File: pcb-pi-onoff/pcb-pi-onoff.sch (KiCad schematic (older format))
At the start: 27 parts, among them J1 Conn_02x20_Odd_Even, J3 Conn_01x06_Male, J4 USB_B_Micro, J5 RUN/~PGM~, J6 Conn_01x03_Male, J7 Conn_SW1, J8 Conn_01x02_Bat, Q1 AO3401A, SW1 SW_Push, U1 TSOP4838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

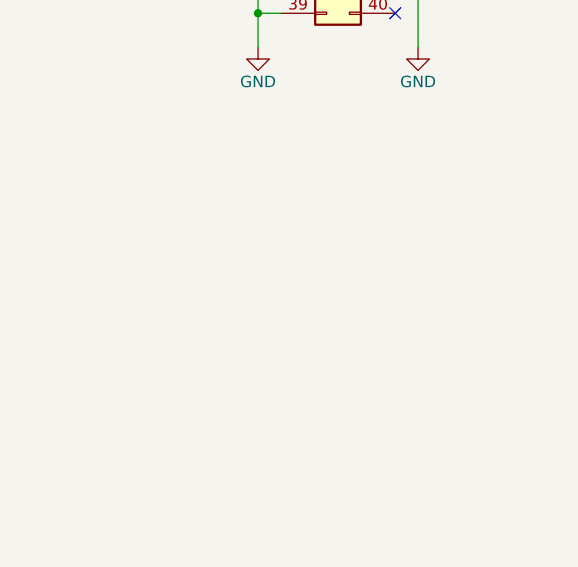
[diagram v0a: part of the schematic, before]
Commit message: added I2C-connector
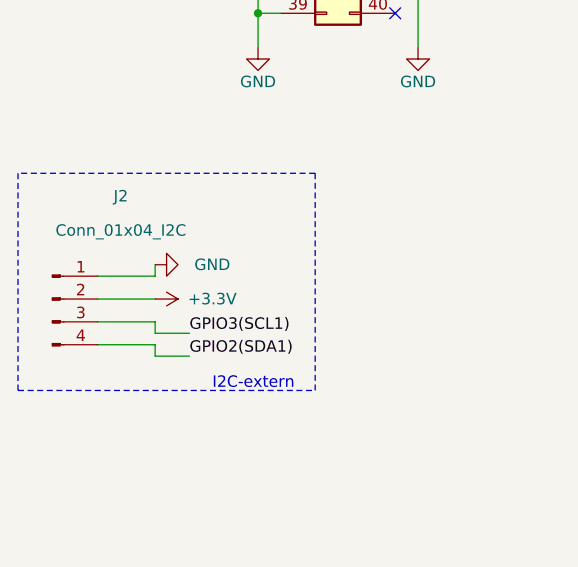
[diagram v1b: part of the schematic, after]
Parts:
- added J2: Conn_01x04_I2C, Connector_PinHeader_2.54mm:PinHeader_1x04_P2.54mm_Vertical, symbol Connector:Conn_01x04_Male
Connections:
- net +3V3: now also J2.2 (Pin_2)
- net GND: now also J2.1 (Pin_1)
- net GPIO2(SDA1): now also J2.4 (Pin_4)
- net GPIO3(SCL1): now also J2.3 (Pin_3)
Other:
- note added: "I2C-extern"
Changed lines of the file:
@@
 $EndComp
 Connection ~ 6100 3100
+$Comp
+L Connector:Conn_01x04_Male J2
+U 1 1 60BFEDEF
+P 800 4100
+F 0 "J2" H 1100 4550 50  0000 C CNN
+F 1 "Conn_01x04_I2C" H 1100 4400 50  0000 C CNN
+F 2 "Connector_PinHeader_2.54mm:PinHeader_1x04_P2.54mm_Vertical" H 800 4100 50  0001 C CNN
+F 3 "~" H 800 4100 50  0001 C CNN
+	1    800  4100
+	1    0    0    -1
+$EndComp
+$Comp
+L power:GND #PWR0106
+U 1 1 60BFFA58
+P 1250 3950
+F 0 "#PWR0106" H 1250 3700 50  0001 C CNN
+F 1 "GND" V 1250 3700 50  0000 C CNN
+F 2 "" H 1250 3950 50  0001 C CNN
+F 3 "" H 1250 3950 50  0001 C CNN
+	1    1250 3950
+	0    -1   -1   0
+$EndComp
+$Comp
+L power:+3.3V #PWR0107
+U 1 1 60C00252
+P 1250 4100
+F 0 "#PWR0107" H 1250 3950 50  0001 C CNN
+F 1 "+3.3V" V 1250 4350 50  0000 C CNN
+F 2 "" H 1250 4100 50  0000 C CNN
+F 3 "" H 1250 4100 50  0000 C CNN
+	1    1250 4100
+	0    1    1    0
+$EndComp
+Text Label 1400 4250 0    50   ~ 0
+GPIO3(SCL1)
+Text Label 1400 4350 0    50   ~ 0
+GPIO2(SDA1)
+Wire Wire Line
+	1000 4000 1250 4000
+Wire Wire Line
+	1000 4100 1250 4100
+Wire Wire Line
+	1000 4200 1250 4200
+Wire Wire Line
+	1250 4200 1250 4250
+Wire Wire Line
+	1000 4300 1250 4300
+Wire Wire Line
+	1250 4300 1250 4350
+Wire Wire Line
+	1250 4000 1250 3950
+Wire Wire Line
+	1250 4250 1400 4250
+Wire Wire Line
+	1250 4350 1400 4350
+Wire Notes Line
+	650  3550 650  4500
+Wire Notes Line
+	650  4500 1950 4500
+Wire Notes Line
+	1950 4500 1950 3550
+Wire Notes Line
+	1950 3550 650  3550
+Text Notes 1500 4500 0    50   ~ 0
+I2C-extern
 $EndSCHEMATC

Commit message: added SPI-connector
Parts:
- added J9: Conn_01x06_SPI, Connector_PinHeader_2.54mm:PinHeader_1x06_P2.54mm_Vertical, symbol Connector:Conn_01x06_Male
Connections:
- net +3V3: now also J9.6 (Pin_6)
- net GND: now also J9.5 (Pin_5)
- net GPIO10(SPI-TX): now reaches J1.19 (Pin_19)
- net GPIO10(SPI-TX): now also J9.3 (Pin_3)
- net GPIO9(SPI-RX): now reaches J1.21 (Pin_21)
- net GPIO9(SPI-RX): now also J9.1 (Pin_1)
- net GPIO11(SPI-CLK): now reaches J1.23 (Pin_23)
- net GPIO11(SPI-CLK): now also J9.4 (Pin_4)
- net GPIO8(SPI-CE0): now reaches J1.24 (Pin_24)
- net GPIO8(SPI-CE0): now also J9.2 (Pin_2)
- no-connect marks 30 -> 26
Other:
- note added: "SPI-extern"
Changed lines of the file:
@@
 NoConn ~ 2300 1750
 NoConn ~ 2300 1950
-NoConn ~ 2300 2050
 NoConn ~ 2300 2150
 NoConn ~ 2300 2250
@@
 NoConn ~ 1800 2350
 NoConn ~ 1800 2250
-NoConn ~ 1800 2050
-NoConn ~ 1800 1950
-NoConn ~ 1800 1850
 NoConn ~ 1800 1650
 NoConn ~ 1800 1550
@@
 Text Notes 1500 4500 0    50   ~ 0
 I2C-extern
+Wire Wire Line
+	650  1850 1800 1850
+Text Label 650  1850 0    50   ~ 0
+GPIO10(SPI-TX)
+Wire Wire Line
+	650  1950 1800 1950
+Text Label 650  1950 0    50   ~ 0
+GPIO9(SPI-RX)
+Wire Wire Line
+	650  2050 1800 2050
+Text Label 650  2050 0    50   ~ 0
+GPIO11(SPI-CLK)
+Wire Wire Line
+	3450 2050 2300 2050
+Text Label 3450 2050 2    50   ~ 0
+GPIO8(SPI-CE0)
+$Comp
+L Connector:Conn_01x06_Male J9
+U 1 1 60C64E02
+P 2500 4100
+F 0 "J9" H 2750 4550 50  0000 C CNN
+F 1 "Conn_01x06_SPI" H 2800 4450 50  0000 C CNN
+F 2 "Connector_PinHeader_2.54mm:PinHeader_1x06_P2.54mm_Vertical" H 2500 4100 50  0001 C CNN
+F 3 "~" H 2500 4100 50  0001 C CNN
+	1    2500 4100
+	1    0    0    -1
+$EndComp
+Text Label 3050 3900 0    50   ~ 0
+GPIO9(SPI-RX)
+Text Label 3050 4000 0    50   ~ 0
+GPIO8(SPI-CE0)
+Text Label 3050 4100 0    50   ~ 0
+GPIO10(SPI-TX)
+Text Label 3050 4200 0    50   ~ 0
+GPIO11(SPI-CLK)
+$Comp
+L power:GND #PWR02
+U 1 1 60C65E52
+P 3050 4300
+F 0 "#PWR02" H 3050 4050 50  0001 C CNN
+F 1 "GND" V 3050 4050 50  0000 C CNN
+F 2 "" H 3050 4300 50  0001 C CNN
+F 3 "" H 3050 4300 50  0001 C CNN
+	1    3050 4300
+	0    -1   -1   0
+$EndComp
+$Comp
+L power:+3.3V #PWR018
+U 1 1 60C6639C
+P 3050 4400
+F 0 "#PWR018" H 3050 4250 50  0001 C CNN
+F 1 "+3.3V" V 3050 4650 50  0000 C CNN
+F 2 "" H 3050 4400 50  0000 C CNN
+F 3 "" H 3050 4400 50  0000 C CNN
+	1    3050 4400
+	0    1    1    0
+$EndComp
+Wire Wire Line
+	2700 3900 3050 3900
+Wire Wire Line
+	2700 4000 3050 4000
+Wire Wire Line
+	2700 4100 3050 4100
+Wire Wire Line
+	2700 4200 3050 4200
+Wire Wire Line
+	2700 4300 3050 4300
+Wire Wire Line
+	2700 4400 3050 4400
+Wire Notes Line
+	2400 3550 2400 4500
+Wire Notes Line
+	2400 4500 3900 4500
+Wire Notes Line
+	3900 4500 3900 3550
+Wire Notes Line
+	3900 3550 2400 3550
+Text Notes 3450 4500 0    50   ~ 0
+SPI-extern
 $EndSCHEMATC

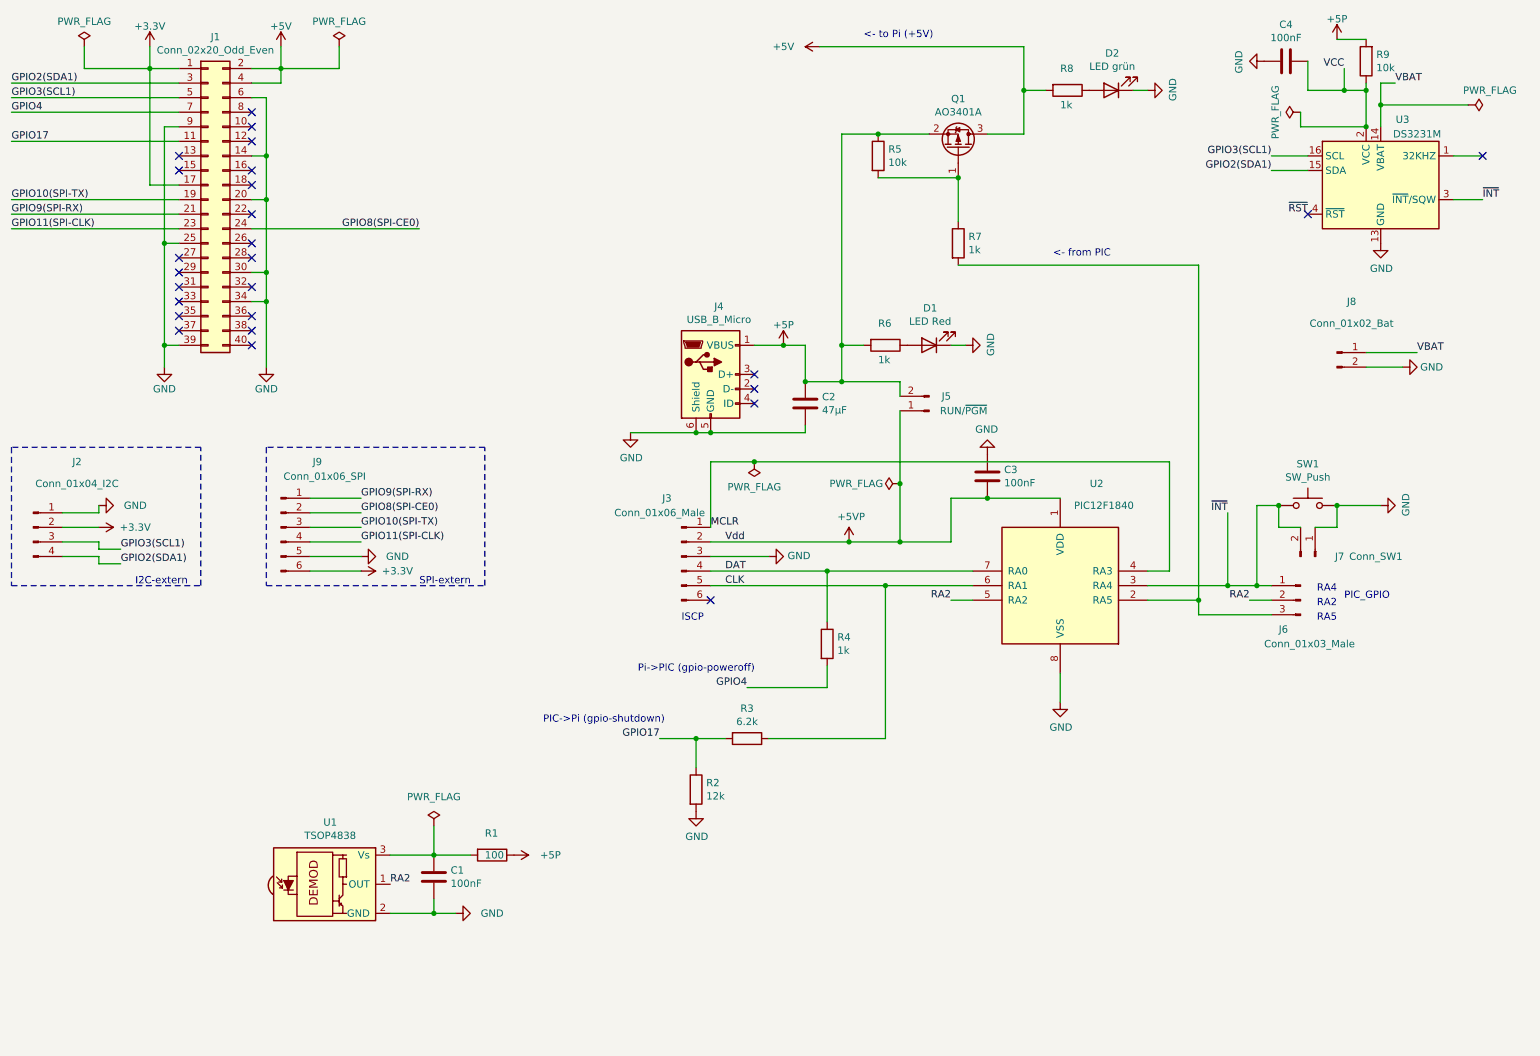
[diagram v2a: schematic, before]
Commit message: added GPIO-connector
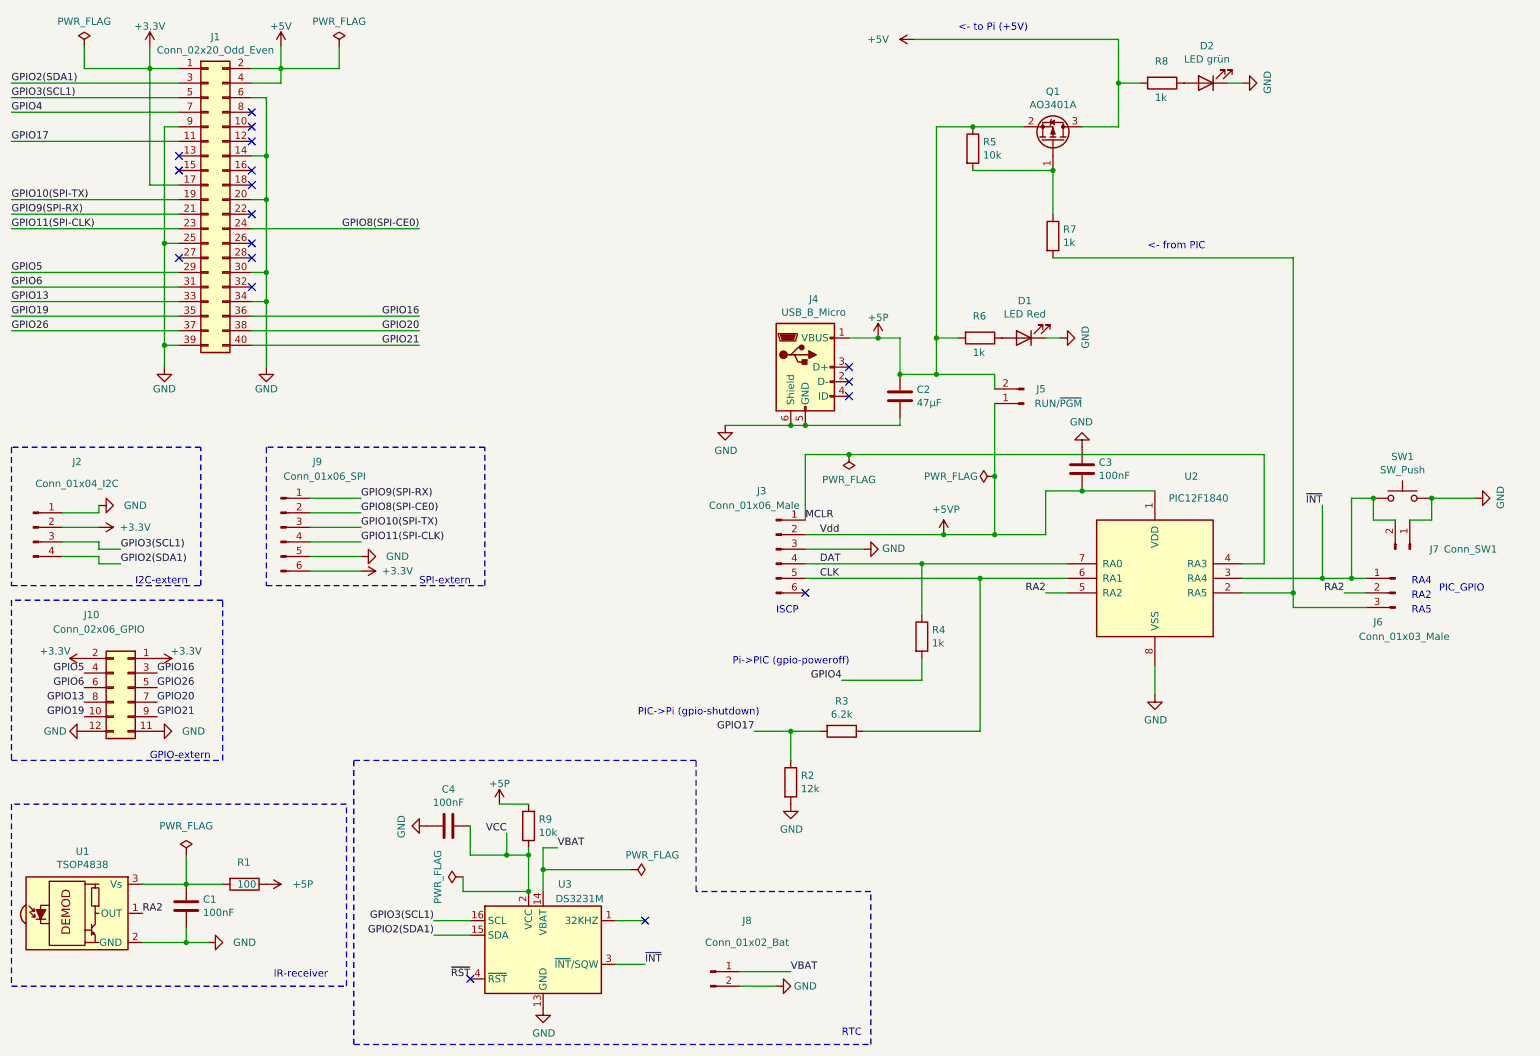
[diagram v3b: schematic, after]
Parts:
- added J10: Conn_02x06_GPIO, Connector_PinHeader_2.54mm:PinHeader_2x06_P2.54mm_Vertical, symbol Connector_Generic:Conn_02x06_Odd_Even
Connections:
- net +3V3: now also J10.1 (Pin_1), J10.2 (Pin_2)
- net GND: now also J10.11 (Pin_11), J10.12 (Pin_12)
- net GPIO5: now reaches J1.29 (Pin_29)
- net GPIO5: now also J10.4 (Pin_4)
- net GPIO6: now reaches J1.31 (Pin_31)
- net GPIO6: now also J10.6 (Pin_6)
- net GPIO13: now reaches J1.33 (Pin_33)
- net GPIO13: now also J10.8 (Pin_8)
- net GPIO19: now reaches J1.35 (Pin_35)
- net GPIO19: now also J10.10 (Pin_10)
- net GPIO16: now reaches J1.36 (Pin_36)
- net GPIO16: now also J10.3 (Pin_3)
- net GPIO26: now reaches J1.37 (Pin_37)
- net GPIO26: now also J10.5 (Pin_5)
- net GPIO20: now reaches J1.38 (Pin_38)
- net GPIO20: now also J10.7 (Pin_7)
- net GPIO21: now reaches J1.40 (Pin_40)
- net GPIO21: now also J10.9 (Pin_9)
- no-connect marks 26 -> 18
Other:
- note added: "GPIO-extern"
- note added: "IR-receiver"
- note added: "RTC"
- moved on the sheet: C1, C2, C3, C4, D1, D2, J3, J4, J5, J6, J7, J8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

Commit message: replaced footprints for PIC and RTC with handsolder-version
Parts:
- U2: footprint Package_SO:SO-8_3.9x4.9mm_P1.27mm -> user:SO-8_3.9x4.9mm_P1.27mm_HandSolder
- U3: footprint Package_SO:SOIC-16W_7.5x10.3mm_P1.27mm -> user:SOIC-16W_7.5x10.3mm_P1.27mm_HandSolder
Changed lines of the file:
@@
 F 0 "U2" H 8750 5150 50  0000 C CNN
 F 1 "PIC12F1840" H 8800 5000 50  0000 C CNN
-F 2 "Package_SO:SO-8_3.9x4.9mm_P1.27mm" H 9100 5100 50  0001 C CNN
+F 2 "user:SO-8_3.9x4.9mm_P1.27mm_HandSolder" H 9100 5100 50  0001 C CNN
 F 3 "" H 8500 4450 50  0001 C CNN
 	1    8500 4450
@@
 F 0 "U3" H 4450 7450 50  0000 C CNN
 F 1 "DS3231M" H 4550 7350 50  0000 C CNN
-F 2 "Package_SO:SOIC-16W_7.5x10.3mm_P1.27mm" H 4300 6400 50  0001 C CNN
+F 2 "user:SOIC-16W_7.5x10.3mm_P1.27mm_HandSolder" H 4300 6400 50  0001 C CNN
 F 3 "http://datasheets.maximintegrated.com/en/ds/DS3231.pdf" H 4570 7050 50  0001 C CNN
 	1    4300 7000

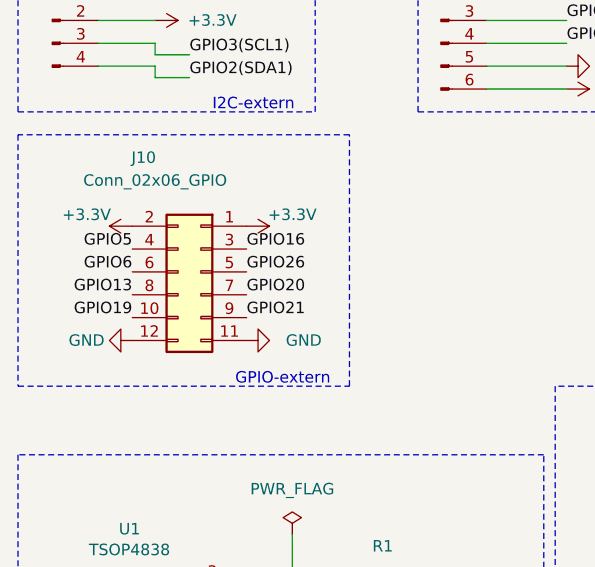
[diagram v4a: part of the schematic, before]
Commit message: Rev 1.0: changed 3V3/GND on GPIO-connector
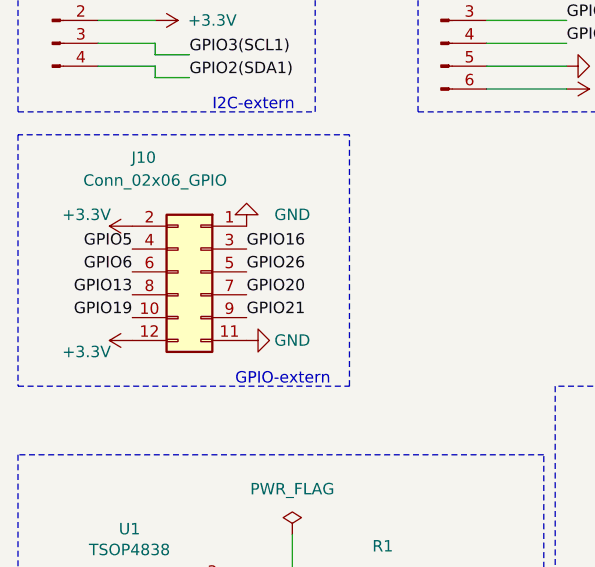
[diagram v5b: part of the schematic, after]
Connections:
- net +3V3: now also J10.12 (Pin_12); no longer J10.1 (Pin_1)
- net GND: now also J10.1 (Pin_1); no longer J10.12 (Pin_12)
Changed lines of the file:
@@
 Sheet 1 1
 Title "Pi OnOff Hat"
-Date "2021-06-08"
-Rev "0.9"
+Date "2021-06-09"
+Rev "1.0"
 Comp "Bernhard Bablok"
 Comment1 "https://github.com/bablokb/pcb-pi-onoff"
@@
 L power:GND #PWR0108
 U 1 1 60D0F918
-P 1150 5500
-F 0 "#PWR0108" H 1150 5250 50  0001 C CNN
-F 1 "GND" V 1150 5300 50  0000 C CNN
-F 2 "" H 1150 5500 50  0001 C CNN
-F 3 "" H 1150 5500 50  0001 C CNN
-	1    1150 5500
-	0    1    1    0
-$EndComp
-$Comp
-L power:GND #PWR0109
-U 1 1 60D0FF1A
 P 1650 5500
-F 0 "#PWR0109" H 1650 5250 50  0001 C CNN
-F 1 "GND" V 1650 5250 50  0000 C CNN
+F 0 "#PWR0108" H 1650 5250 50  0001 C CNN
+F 1 "GND" V 1650 5300 50  0000 C CNN
 F 2 "" H 1650 5500 50  0001 C CNN
 F 3 "" H 1650 5500 50  0001 C CNN
@@
 $EndComp
 $Comp
+L power:GND #PWR0109
+U 1 1 60D0FF1A
+P 1650 5000
+F 0 "#PWR0109" H 1650 4750 50  0001 C CNN
+F 1 "GND" H 1450 4950 50  0000 C CNN
+F 2 "" H 1650 5000 50  0001 C CNN
+F 3 "" H 1650 5000 50  0001 C CNN
+	1    1650 5000
+	-1   0    0    1
+$EndComp
+$Comp
 L power:+3.3V #PWR0110
 U 1 1 60D108D6
-P 1650 5000
-F 0 "#PWR0110" H 1650 4850 50  0001 C CNN
-F 1 "+3.3V" V 1600 5200 50  0000 C CNN
-F 2 "" H 1650 5000 50  0000 C CNN
-F 3 "" H 1650 5000 50  0000 C CNN
-	1    1650 5000
-	0    1    1    0
-$EndComp
-$Comp
+P 1150 5500
+F 0 "#PWR0110" H 1150 5350 50  0001 C CNN
+F 1 "+3.3V" V 1100 5700 50  0000 C CNN
+F 2 "" H 1150 5500 50  0000 C CNN
+F 3 "" H 1150 5500 50  0000 C CNN
+	1    1150 5500
+	0    -1   -1   0
+$EndComp
+$Comp
